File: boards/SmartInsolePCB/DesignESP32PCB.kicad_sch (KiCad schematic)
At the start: 44 parts, among them J2 Conn_01x02_Socket, J4 Conn_01x02_Socket, J5 Conn_01x02_Socket, J6 Conn_01x02_Socket, J7 Conn_01x02_Socket, J8 Conn_01x02_Socket, SW1 SW_Push, SW2 SW_Push, U1 ESP32-S3-MINI-1-N8, U2 D3V3XA4B10LP, U3 TLV75801PDRV, U4 SN74LVC1G14DBV, U5 SN74LVC1G14DBV

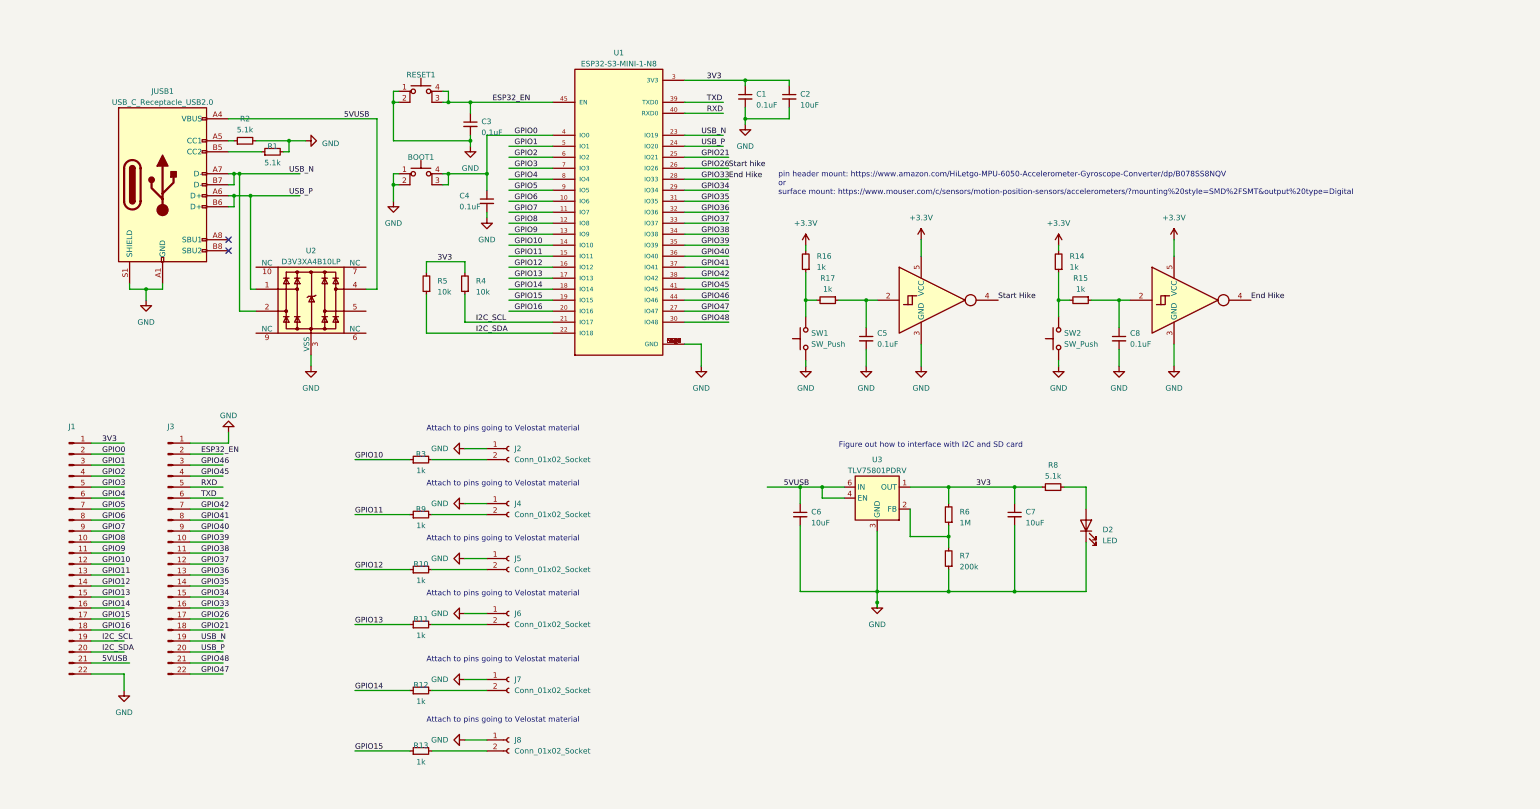
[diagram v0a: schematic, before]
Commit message: added 6050, added footprints
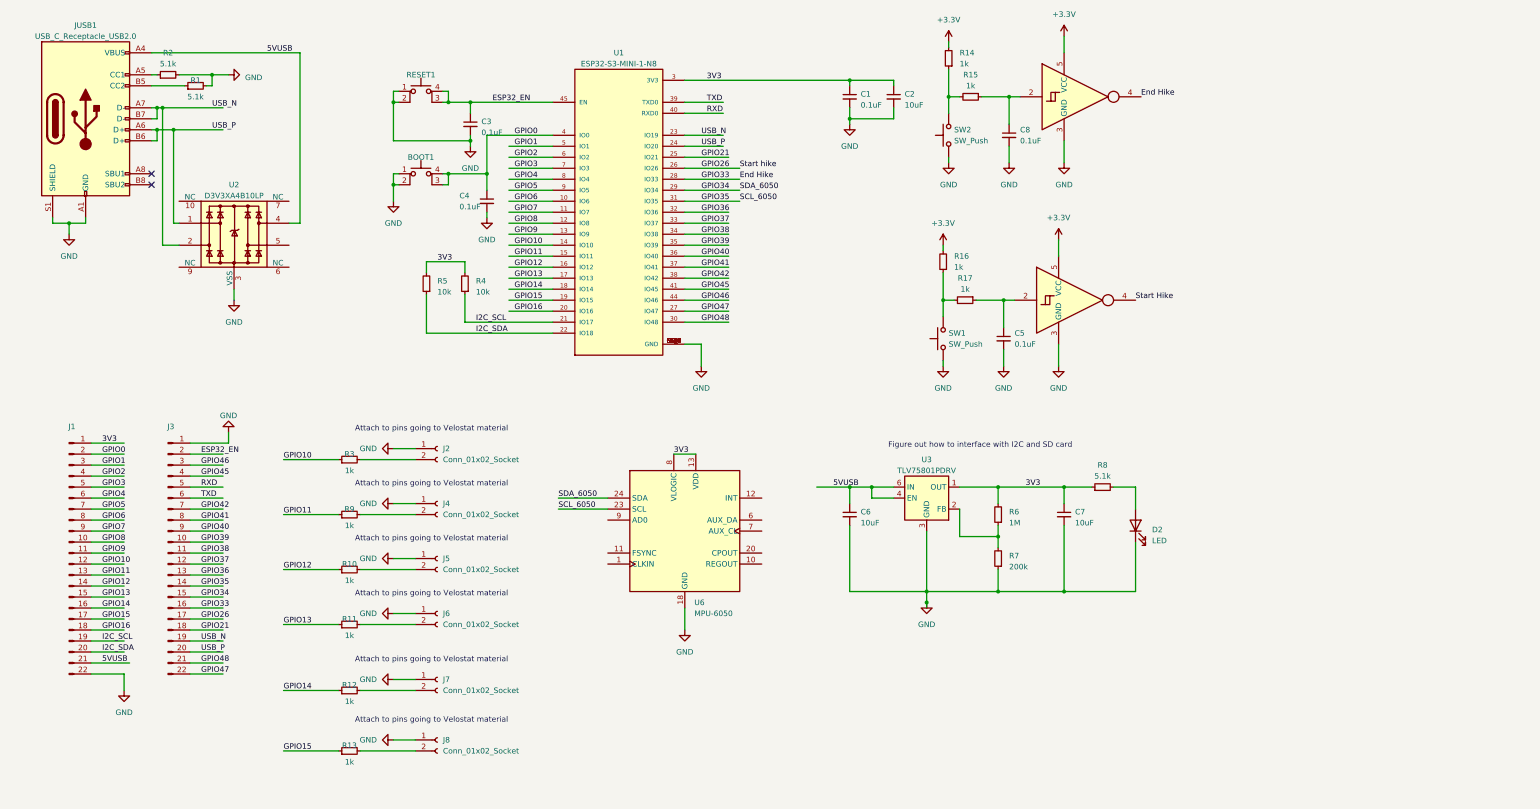
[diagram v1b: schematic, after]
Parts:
- added U6: MPU-6050, Sensor_Motion:InvenSense_QFN-24_4x4mm_P0.5mm, symbol Sensor_Motion:MPU-6050
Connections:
- net 3V3: now also U6.13 (VDD), U6.8 (VLOGIC)
- net GND: now also U6.18 (GND)
- net GPIO34: now also U6.24 (SDA)
- net GPIO35: now also U6.23 (SCL)
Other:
- note removed: "pin header mount: https://www.amazon.com/HiLetgo-MPU-6050-Accelerometer-Gyroscope-Converter/dp/B078SS8NQV or surface mount: https://www.mouser.com/c/sensors/motion-position-sensors/accelerometers/?mounting%20style=SMD%2FSMT&output%20type=Digital"
- moved on the sheet: C1, C2, C5, C6, C7, C8, D2, J2, J4, J5, J6, J7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

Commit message: added SD card Pin headers
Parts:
- removed J1, J3: ~, symbol Connector:Conn_01x22_Pin
- added J1: Conn_01x06_Socket, symbol Connector:Conn_01x06_Socket
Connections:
- net +3.3V: now also J1.1 (Pin_1)
- net GND: now also J1.6 (Pin_6)
- net GPIO45: now also J1.4 (Pin_4)
- net GPIO47: now also J1.3 (Pin_3)
- net GPIO48: now also J1.5 (Pin_5)
- net GPIO46 renamed CS
- net CS: now also J1.2 (Pin_2)
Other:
- company: (none) -> Group 41
- title: (none) -> Smart Insole PCB Design

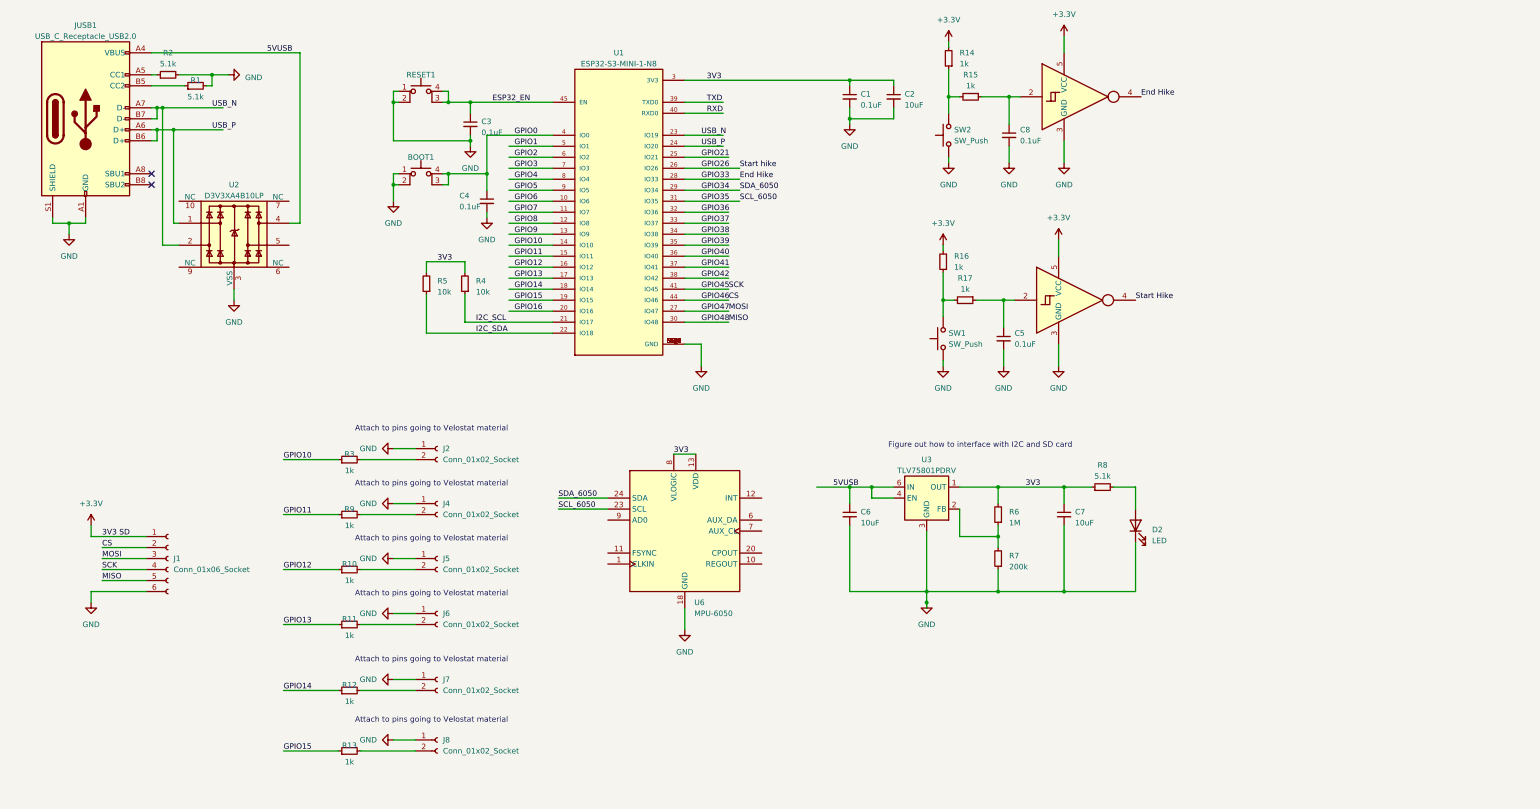
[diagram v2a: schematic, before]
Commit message: replaced ESP32 symbol
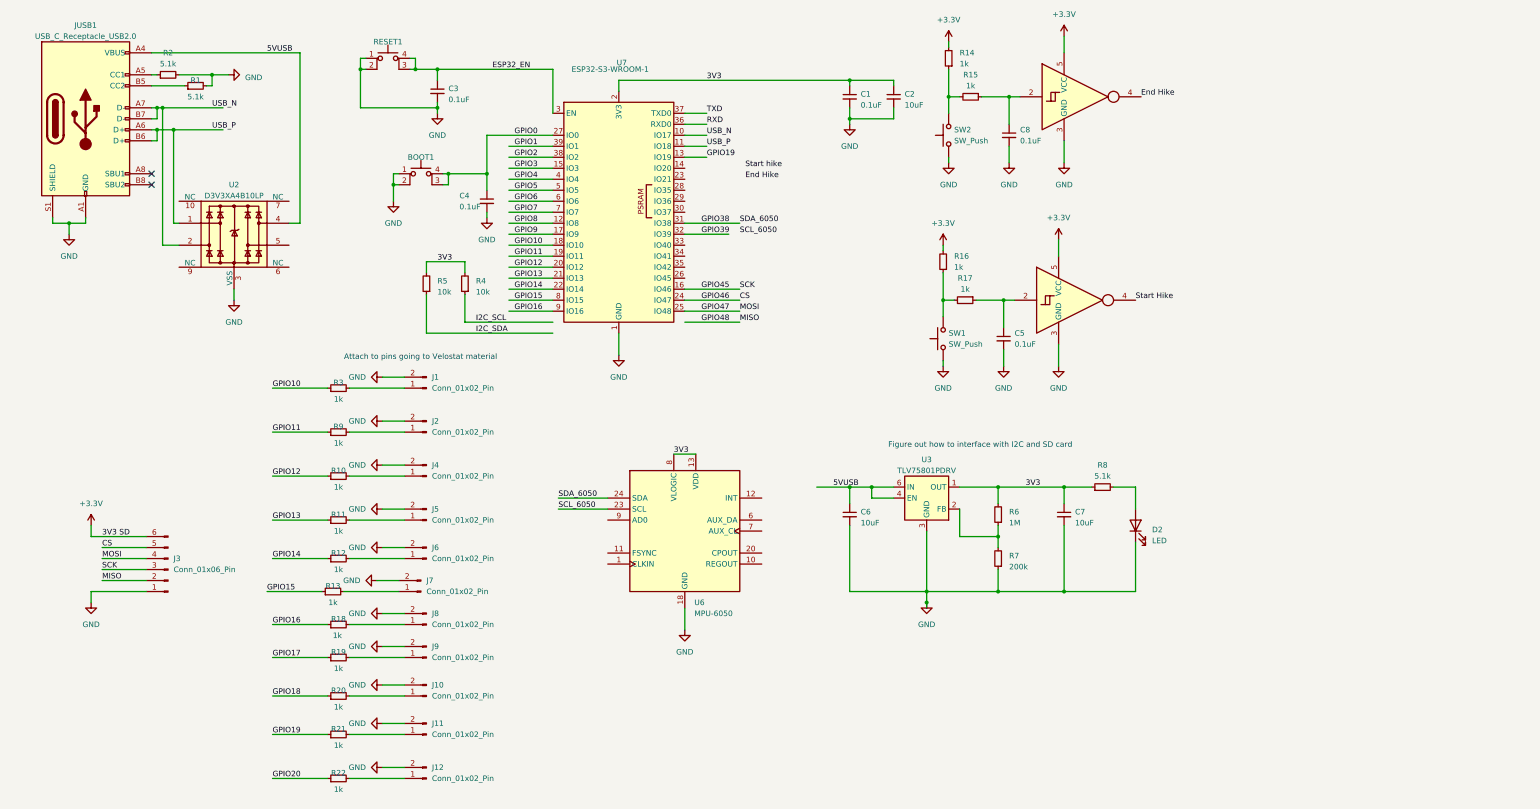
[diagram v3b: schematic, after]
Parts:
- removed J1: Conn_01x06_Socket, symbol Connector:Conn_01x06_Socket
- removed J2, J4, J5, J6, J7, J8: Conn_01x02_Socket, symbol Connector:Conn_01x02_Socket
- removed U1: ESP32-S3-MINI-1-N8, ESP32-S3-MINI-1-N8:XCVR_ESP32-S3-MINI-1-N8, symbol ESP32-S3-MINI-1-N8:ESP32-S3-MINI-1-N8
- added J1, J10, J11, J12, J2, J4, J5, J6, J7, J8, J9: Conn_01x02_Pin, Connector_PinHeader_1.00mm:PinHeader_1x02_P1.00mm_Vertical, symbol Connector:Conn_01x02_Pin
- added J3: Conn_01x06_Pin, Connector_PinHeader_1.00mm:PinHeader_1x06_P1.00mm_Vertical, symbol Connector:Conn_01x06_Pin
- added R18, R19, R20, R21, R22: 1k, Resistor_SMD:R_0603_1608Metric, symbol Device:R_Small
- added U7: ESP32-S3-WROOM-1, RF_Module:ESP32-S3-WROOM-1, symbol RF_Module:ESP32-S3-WROOM-1
- BOOT1, RESET1: footprint Button_Switch_SMD:SW_SPST_PTS810 -> Button_Switch_SMD:SW_Push_1P1T_NO_CK_PTS125Sx43PSMTR
- SW1, SW2: footprint (none) -> Button_Switch_SMD:SW_Push_1P1T_NO_CK_PTS125Sx43PSMTR
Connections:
- net GPIO34 is gone; now on net GPIO38: U6.24 (SDA)
- net +3.3V: now also J3.6 (Pin_6)
- net 3V3: now also U7.2 (3V3)
- net CS: now also J3.5 (Pin_5), U7.24 (IO47)
- net ESP32_EN: now also U7.3 (EN)
- net GND: now also J1.2 (Pin_2), J10.2 (Pin_2), J11.2 (Pin_2), J12.2 (Pin_2), J2.2 (Pin_2), J3.1 (Pin_1), J4.2 (Pin_2), J5.2 (Pin_2), J6.2 (Pin_2), J7.2 (Pin_2), J8.2 (Pin_2), J9.2 (Pin_2), U7.1 (GND), U7.40 (GND), U7.41 (GND)
- net GPIO0: now also U7.27 (IO0)
- net GPIO1: now also U7.39 (IO1)
- net GPIO10: now also U7.18 (IO10)
- net GPIO11: now also U7.19 (IO11)
- net GPIO12: now also U7.20 (IO12)
- net GPIO13: now also U7.21 (IO13)
- net GPIO14: now also U7.22 (IO14)
- net GPIO15: now also U7.8 (IO15)
- net GPIO16: now also R18.1, U7.9 (IO16)
- net GPIO2: now also U7.38 (IO2)
- net GPIO3: now also U7.15 (IO3)
- net GPIO38: now also U7.31 (IO38)
- net GPIO39: now also U7.32 (IO39)
- net GPIO4: now also U7.4 (IO4)
- net GPIO45: now also J3.3 (Pin_3), U7.16 (IO46)
- net GPIO47: now also J3.4 (Pin_4), U7.25 (IO48)
- net GPIO48: now also J3.2 (Pin_2)
- net GPIO5: now also U7.5 (IO5)
- net GPIO6: now also U7.6 (IO6)
- net GPIO7: now also U7.7 (IO7)
- net GPIO8: now also U7.12 (IO8)
- net GPIO9: now also U7.17 (IO9)
- net RXD: now also U7.36 (RXD0)
- net TXD: now also U7.37 (TXD0)
- net USB_N: now also U7.10 (IO17)
- net USB_P: now also U7.11 (IO18)
- net at R3.2: now also J1.1 (Pin_1)
- net at R13.2: now also J7.1 (Pin_1)
- net at R10.2: now also J4.1 (Pin_1)
- net at R9.2: now also J2.1 (Pin_1)
- net at R11.2: now also J5.1 (Pin_1)
- net at R12.2: now also J6.1 (Pin_1)
- net GPIO35 renamed SCL_6050
- new net: J11.1 (Pin_1), R21.2
- new net: J10.1 (Pin_1), R20.2
- new net: J9.1 (Pin_1), R19.2
- new net: J8.1 (Pin_1), R18.2
- new net: J12.1 (Pin_1), R22.2
- new net GPIO17: R19.1
- new net GPIO18: R20.1
- new net GPIO19: R21.1, U7.13 (IO19)
- new net GPIO20: R22.1
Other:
- moved on the sheet: C3, R3, RESET1

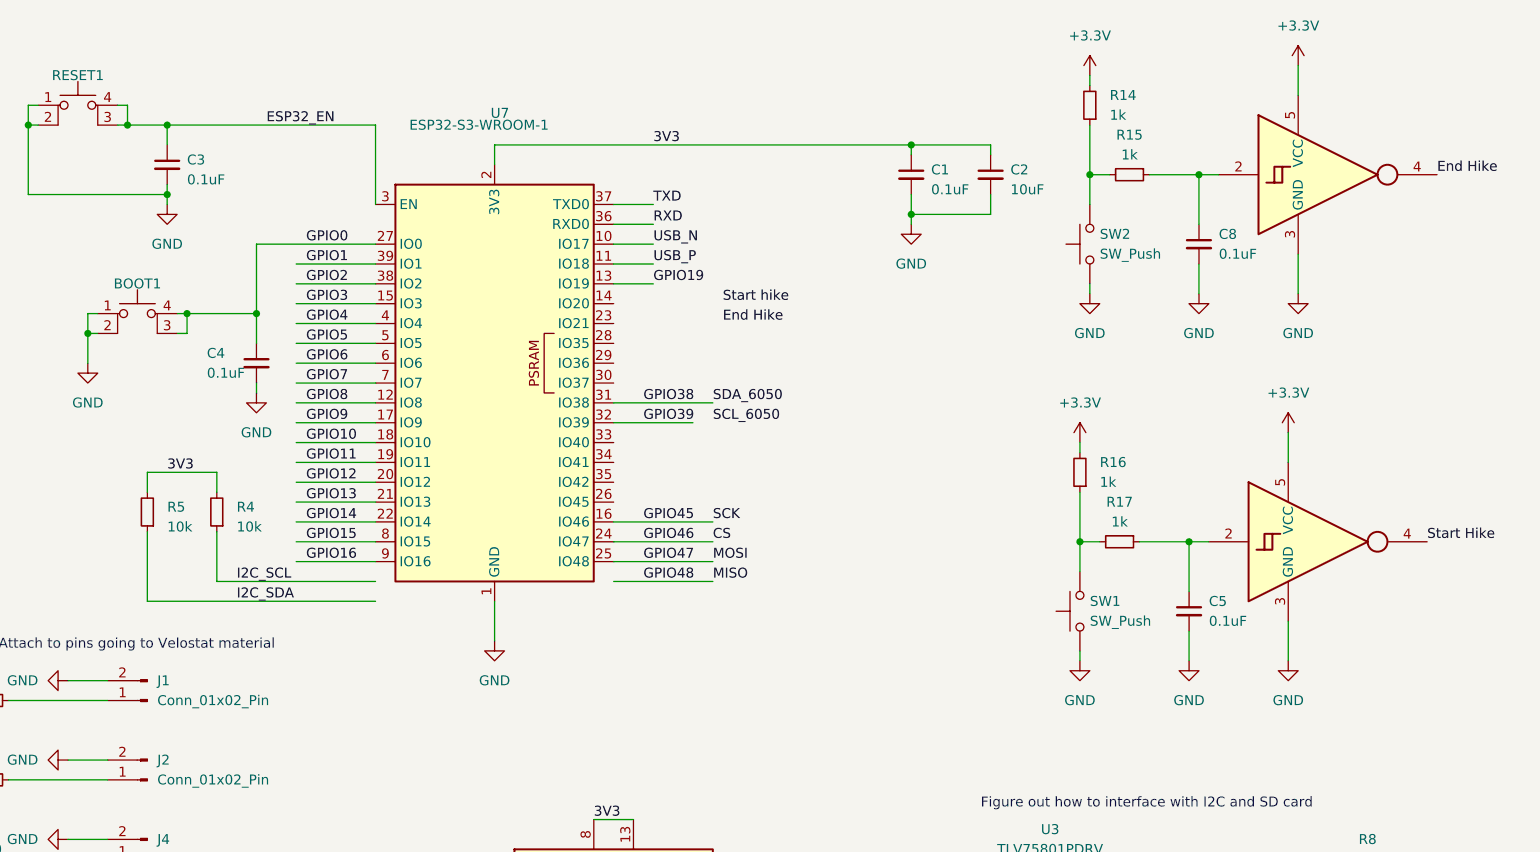
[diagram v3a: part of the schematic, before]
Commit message: debounced buttons and connected pins
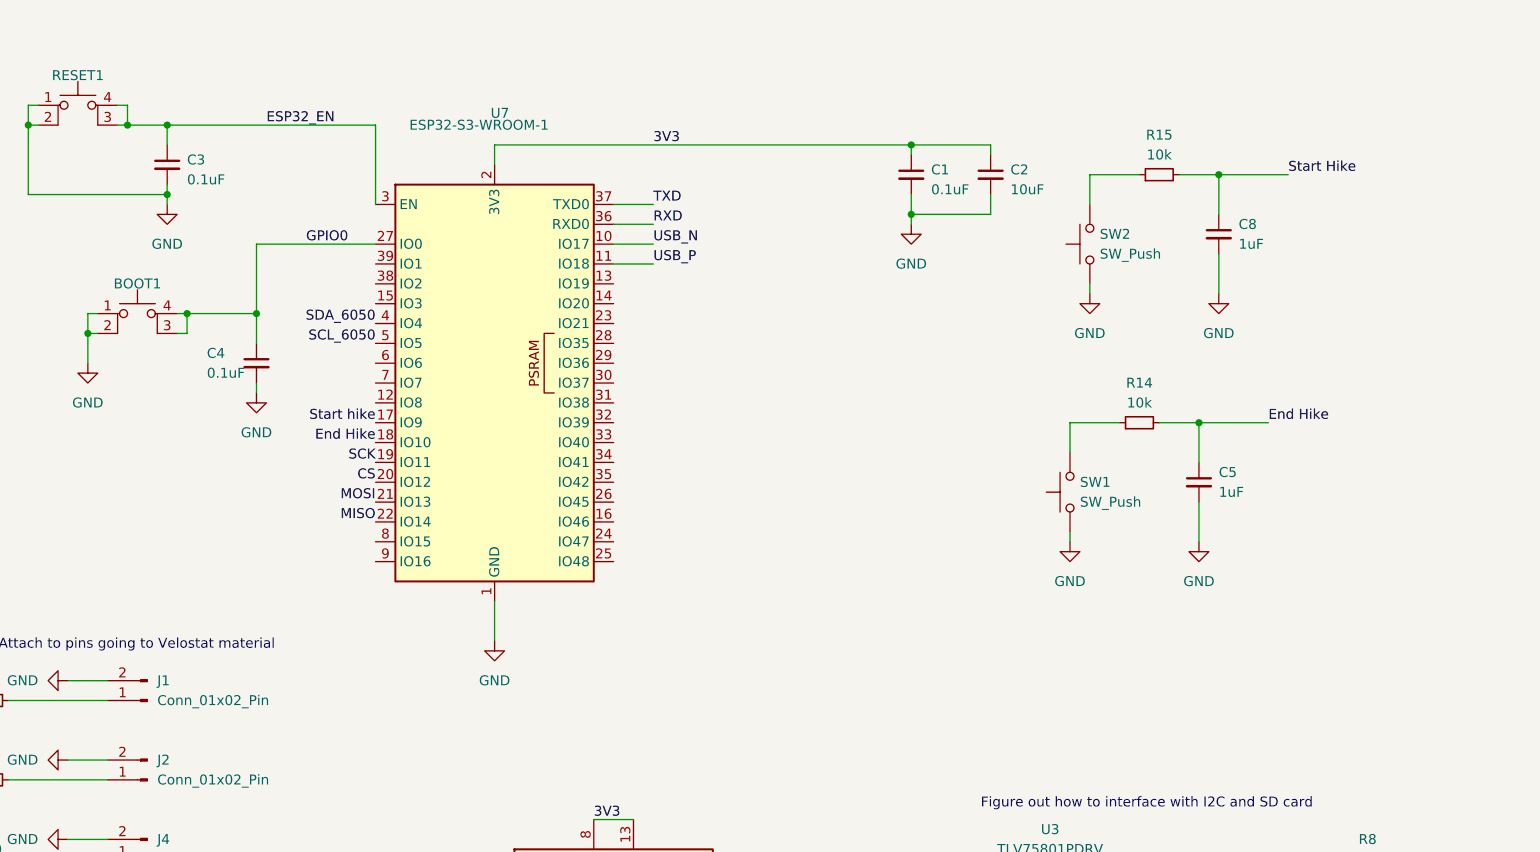
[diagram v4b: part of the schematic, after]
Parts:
- removed R16, R17: 1k, Resistor_SMD:R_0603_1608Metric, symbol Device:R_Small
- removed R4, R5: 10k, Resistor_SMD:R_0603_1608Metric, symbol Device:R_Small
- removed U4, U5: SN74LVC1G14DBV, Package_TO_SOT_SMD:SOT-23-5, symbol 74xGxx:SN74LVC1G14DBV
- C5, C8: value 0.1uF -> 1uF
- R14, R15: value 1k -> 10k
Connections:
- net GPIO5 is gone; now on net SCL_6050: U7.5 (IO5)
- net GPIO9 is gone; now on net Start hike: U7.17 (IO9)
- net +3.3V: no longer R14.2
- net CS: now also U7.20 (IO12); no longer U7.24 (IO47)
- net End Hike: now also C5.1, R14.2, U7.18 (IO10)
- net GPIO10: no longer U7.18 (IO10)
- net GPIO11: no longer U7.19 (IO11)
- net GPIO12: no longer U7.20 (IO12)
- net GPIO13: no longer U7.21 (IO13)
- net GPIO14: no longer U7.22 (IO14)
- net GPIO15: no longer U7.8 (IO15)
- net GPIO16: no longer U7.9 (IO16)
- net GPIO19: no longer U7.13 (IO19)
- net Start Hike: now also C8.1, R15.2
- net at R15.1: now also SW2.2; no longer C8.1
- net at SW1.2: now also R14.1
- net GPIO1: no longer names the net of U7.39 (IO1)
- net GPIO2: no longer names the net of U7.38 (IO2)
- net GPIO3: no longer names the net of U7.15 (IO3)
- net GPIO38: no longer names the net of U7.31 (IO38)
- net GPIO38: no longer U6.24 (SDA)
- net GPIO39: no longer names the net of U7.32 (IO39)
- net GPIO4 renamed SDA_6050
- net SDA_6050: now also U6.24 (SDA)
- net GPIO45: no longer names the net of U7.16 (IO46)
- net GPIO45: no longer J3.3 (Pin_3)
- net GPIO47: no longer names the net of U7.25 (IO48)
- net GPIO47: no longer J3.4 (Pin_4)
- net GPIO48 renamed MISO
- net MISO: now also U7.22 (IO14)
- net GPIO6: no longer names the net of U7.6 (IO6)
- net GPIO7: no longer names the net of U7.7 (IO7)
- net GPIO8: no longer names the net of U7.12 (IO8)
- new net MOSI: J3.4 (Pin_4), U7.21 (IO13)
- new net SCK: J3.3 (Pin_3), U7.19 (IO11)
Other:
- moved on the sheet: R15
